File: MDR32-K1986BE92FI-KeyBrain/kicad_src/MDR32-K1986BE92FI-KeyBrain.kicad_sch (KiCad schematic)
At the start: 0 parts

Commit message: MDR32-K1986BE92FI-KeyBrain: * выравниваем библиотеки * питание и USB в УГО
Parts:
- added C1, C4, C5, C6: 0.1μF, symbol Device:C
- added C2: 1μF, symbol Device:C
- added C3: 10μF, symbol Device:C
- added D1: LED, symbol Device:LED
- added D2: K1986BE92FI, Package_DFN_QFN:QFN-64-1EP_9x9mm_P0.5mm_EP7.5x7.5mm, symbol MDR32-K1986BE92FI-KeyBrain:K1986BE92FI
- added J1, J2: Conn_01x12, symbol Connector_Generic:Conn_01x12
- added J3: USB_C_Receptacle_USB2.0_16P, symbol Connector:USB_C_Receptacle_USB2.0_16P
- added R1, R2: 5.1K, symbol Device:R
- added R3, R4: 10K, symbol Device:R
- added U1: USBLC6-2SC6, Package_TO_SOT_SMD:SOT-23-6, symbol Power_Protection:USBLC6-2SC6
- added U2: AP2112K-3.3, Package_TO_SOT_SMD:SOT-23-5, symbol Regulator_Linear:AP2112K-3.3
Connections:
- new net: J3.A5 (CC1), R2.1
- new net: J3.A7 (D-), J3.B7 (D-), U1.1 (I/O1)
- new net: J3.A6 (D+), J3.B6 (D+), U1.3 (I/O2)
- new net: J3.B5 (CC2), R1.1
- new net +3.3V: C3.1, C4.1, C5.1, C6.1, D1.2 (A), D2.1 (UCC), D2.12 (UCC), D2.13 (BUCC), D2.24 (AUCC1), D2.28 (AUCC), D2.38 (UCC), D2.48 (UCC), R3.1, R4.1, U2.5 (VOUT)
- new net GND: C1.2, C2.2, C3.2, C4.2, C5.2, C6.2, D1.1 (K), D2.11 (GND), D2.23 (AGND1), D2.27 (AGND), D2.39 (GND), D2.49 (GND), D2.6 (PF4), D2.64 (GND), D2.65 (PAD), D2.7 (PF5), D2.8 (PF6), J3.A1 (GND), J3.A12 (GND), J3.B1 (GND), J3.B12 (GND), R1.2, R2.2, U1.2 (GND), U2.2 (GND)
- new net JBTCK: D2.32 (PD1), R4.2
- new net JBTMS: D2.31 (PD0), R3.2
- new net USBDM: D2.10 (DN), U1.6 (I/O1)
- new net USBDP: D2.9 (DP), U1.4 (I/O2)
- new net VBUS: C1.1, C2.1, J3.A4 (VBUS), J3.A9 (VBUS), J3.B4 (VBUS), J3.B9 (VBUS), U1.5 (VBUS), U2.1 (VIN), U2.3 (EN)
- no-connect marks 0 -> 4
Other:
- note added: "*1"
- note added: "*1 Шунтирующие конденсаторы, обязательно около VCC, AVCC и AVCC1 *2 Доступен только режим JTAG_B *? возможно лучше JTAG_B заменить на JTAG_A чтобы аналоговый порт был доступен целиком в таком случае, в случае глюков МК, не возможно будет его восстановить"
- note added: "*2"

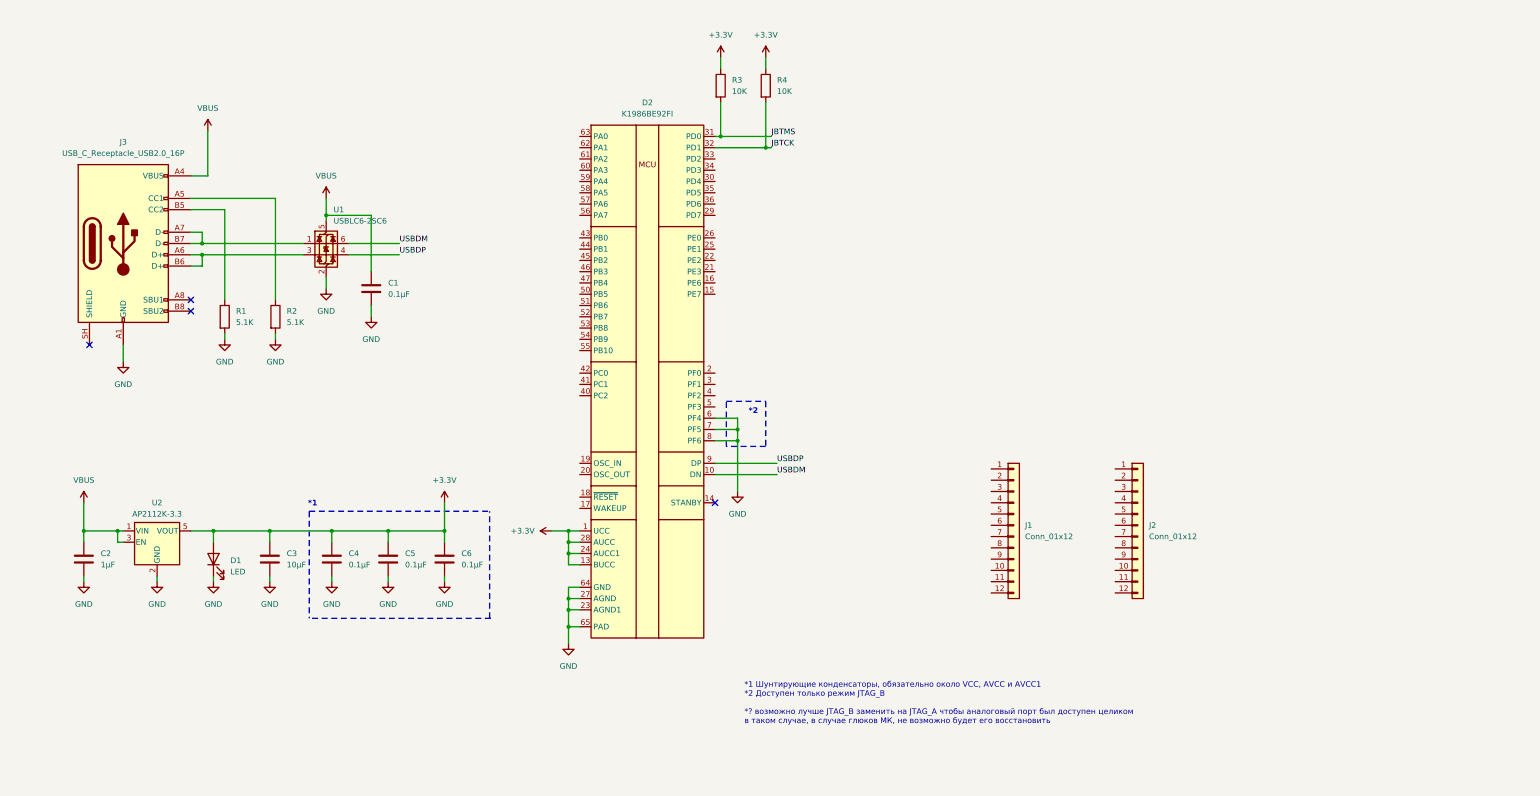
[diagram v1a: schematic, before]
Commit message: update schematic for KeyBrain
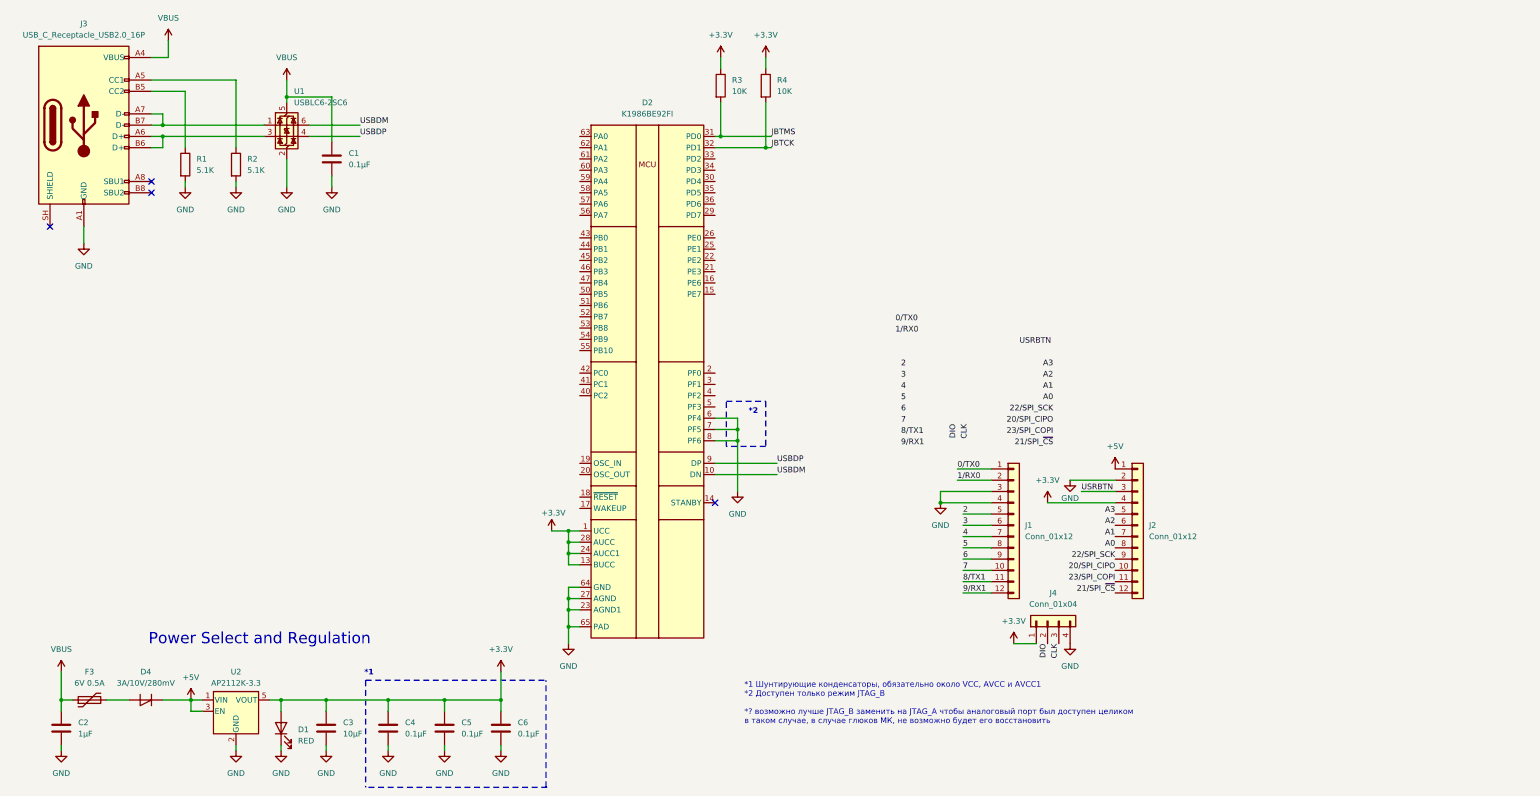
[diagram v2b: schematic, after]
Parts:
- added D4: 3A/10V/280mV, symbol Device:D_Shockley
- added F3: 6V 0.5A, symbol Device:Polyfuse
- added J4: Conn_01x04, symbol Connector_Generic:Conn_01x04
- D1: value LED -> RED
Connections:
- net +3.3V: now also J2.4 (Pin_4), J4.1 (Pin_1)
- net GND: now also J1.3 (Pin_3), J1.4 (Pin_4), J2.2 (Pin_2), J4.4 (Pin_4)
- net VBUS: now also F3.1; no longer U2.1 (VIN), U2.3 (EN)
- net 0/TX0: now reaches J1.1 (Pin_1)
- net 7: now reaches J1.10 (Pin_10)
- net 8/TX1: now reaches J1.11 (Pin_11)
- net 9/RX1: now reaches J1.12 (Pin_12)
- net 1/RX0: now reaches J1.2 (Pin_2)
- net 2: now reaches J1.5 (Pin_5)
- net 3: now reaches J1.6 (Pin_6)
- net 4: now reaches J1.7 (Pin_7)
- net 5: now reaches J1.8 (Pin_8)
- net 6: now reaches J1.9 (Pin_9)
- net +5V: now reaches J2.1 (Pin_1)
- net +5V: now also U2.1 (VIN), U2.3 (EN), D4.1 (K)
- net 20/SPI_CIPO: now reaches J2.10 (Pin_10)
- net 23/SPI_COPI: now reaches J2.11 (Pin_11)
- net 21/SPI_~{CS}: now reaches J2.12 (Pin_12)
- net USRBTN: now reaches J2.3 (Pin_3)
- net A3: now reaches J2.5 (Pin_5)
- net A2: now reaches J2.6 (Pin_6)
- net A1: now reaches J2.7 (Pin_7)
- net A0: now reaches J2.8 (Pin_8)
- net 22/SPI_SCK: now reaches J2.9 (Pin_9)
- new net: D4.2 (A), F3.2
- new net CLK: J4.3 (Pin_3)
- new net DIO: J4.2 (Pin_2)
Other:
- note added: "Power Select and Regulation"
- moved on the sheet: C1, C2, C3, C4, C5, C6, D1, J3, R1, R2, U1, U2

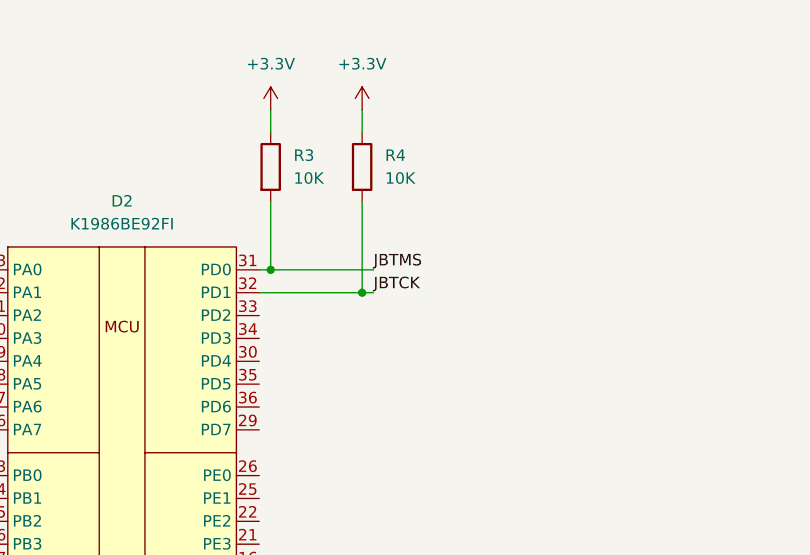
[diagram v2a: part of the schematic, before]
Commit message: MDR32-K1986BE92FI-KeyBrain: более явные имена у пинов для SWD
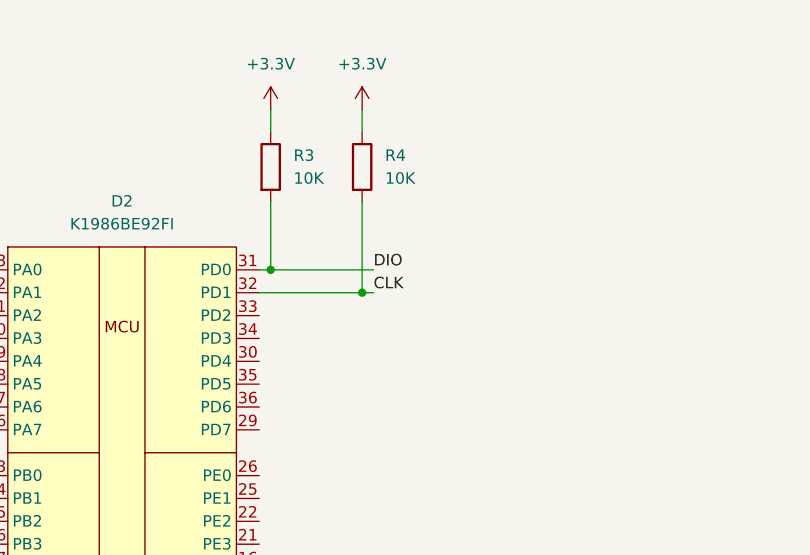
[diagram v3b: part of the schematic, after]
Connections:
- net JBTCK is gone; now on net CLK: D2.32 (PD1), R4.2
- net JBTMS is gone; now on net DIO: D2.31 (PD0), R3.2
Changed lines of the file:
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@@
 		)
 	)
-	(label "JBTCK"
+	(label "CLK"
 		(at 184.15 46.99 0)
 		(effects
@@
 		)
 	)
-	(label "JBTMS"
+	(label "DIO"
 		(at 184.15 44.45 0)
 		(effects

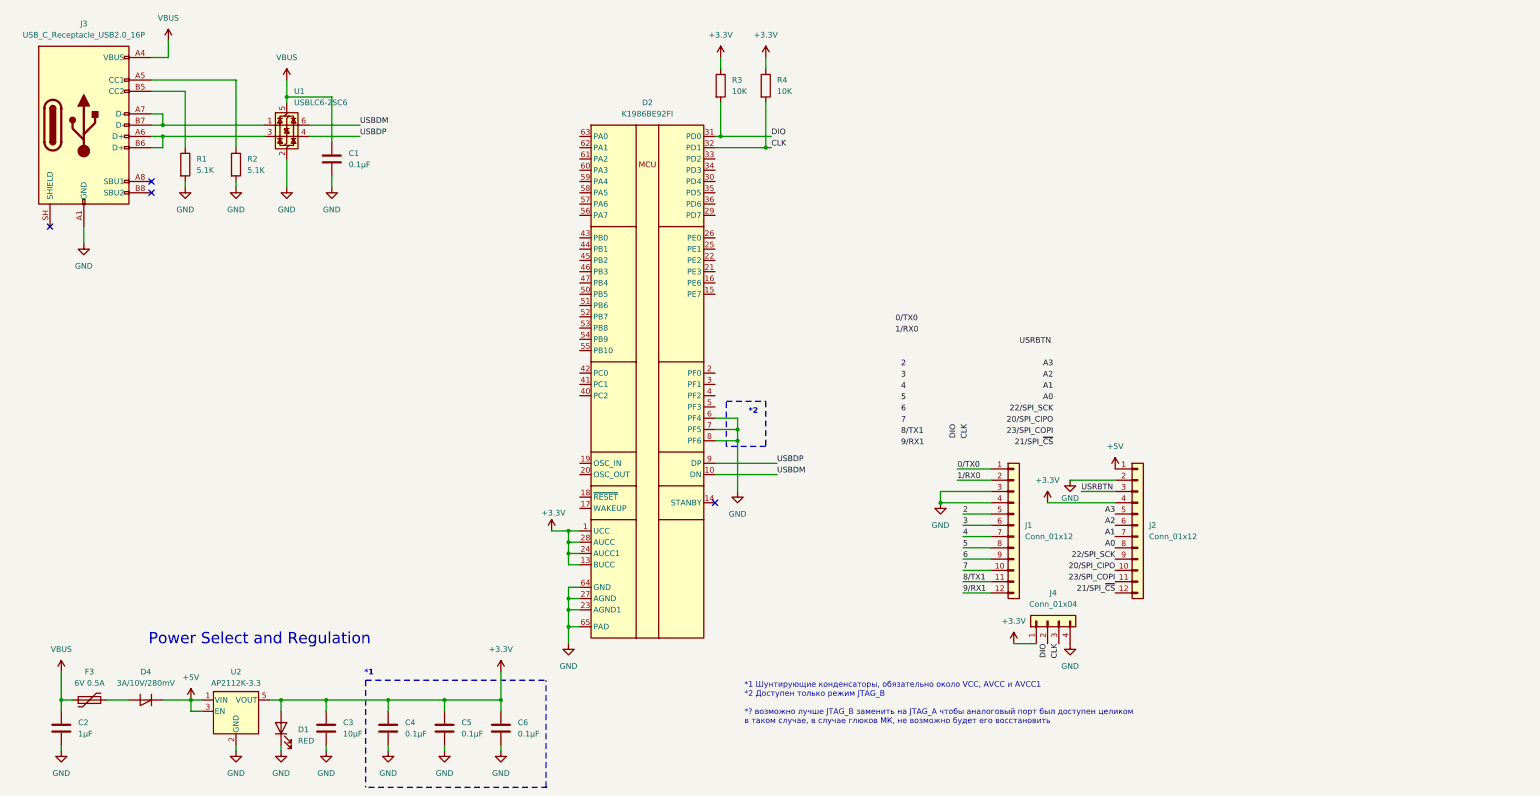
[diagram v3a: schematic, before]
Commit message: MDR32-K1986BE92FI-KeyBrain: резистивная подтяжка сервисных пинов
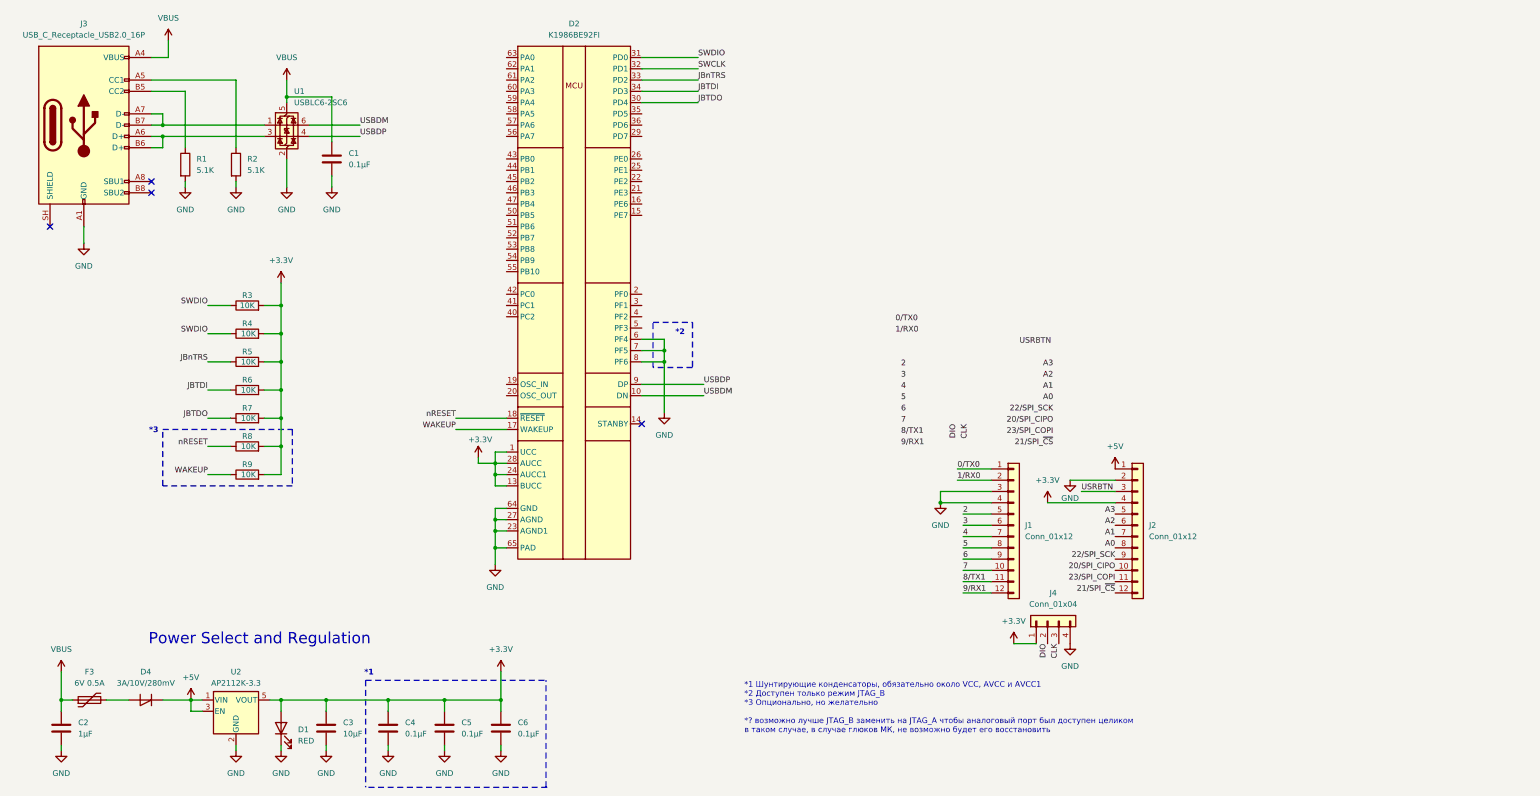
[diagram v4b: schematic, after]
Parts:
- added R5, R6, R7, R8, R9: 10K, symbol Device:R
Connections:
- net +3.3V: now also R3.2, R4.2, R5.2, R6.2, R7.2, R8.2, R9.2; no longer R3.1, R4.1
- net CLK: no longer D2.32 (PD1), R4.2
- net DIO: no longer D2.31 (PD0), R3.2
- net WAKEUP: now reaches D2.17 (WAKEUP)
- net WAKEUP: now also R9.1
- net nRESET: now reaches D2.18 (~{RESET})
- net nRESET: now also R8.1
- net JBTDO: now reaches D2.30 (PD4)
- net JBTDO: now also R7.1
- net JBnTRS: now reaches D2.33 (PD2)
- net JBnTRS: now also R5.1
- net JBTDI: now reaches D2.34 (PD3)
- net JBTDI: now also R6.1
- new net SWCLK: D2.32 (PD1)
- new net SWDIO: D2.31 (PD0), R3.1, R4.1
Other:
- note added: "*1 Шунтирующие конденсаторы, обязательно около VCC, AVCC и AVCC1 *2 Доступен только режим JTAG_B *3 Опционально, но желательно *? возможно лучше JTAG_B заменить на JTAG_A чтобы аналоговый порт был доступен целиком в таком случае, в случае глюков МК, не возможно будет его восстановить"
- note added: "*3"
- note removed: "*1 Шунтирующие конденсаторы, обязательно около VCC, AVCC и AVCC1 *2 Доступен только режим JTAG_B *? возможно лучше JTAG_B заменить на JTAG_A чтобы аналоговый порт был доступен целиком в таком случае, в случае глюков МК, не возможно будет его восстановить"
- moved on the sheet: D2, R3, R4
